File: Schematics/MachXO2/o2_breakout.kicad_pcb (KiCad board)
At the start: 2 copper layers, 95 x 72 mm, 94 parts, among them J1 Conn_02x20_Odd_Even, J2 Conn_02x20_Odd_Even, J3 USB_B_Micro, J4 DM3AT-SF-PEJM5, SW3 Reset, U1 LCMXO2-2000HC-4TG100C, U2 FT2232D, U3 TCM809, U4 93C56, U5 CY7C1010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

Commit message: Update Schematic
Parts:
- C6: moved to F.Cu
- U4: footprint Housings_SOIC:SO-8_5.3x6.2mm_Pitch1.27mm -> Housings_SOIC:SOIC-8_3.9x4.9mm_Pitch1.27mm
- U9: footprint Package_SO:SOIC-8_5.23x5.23mm_P1.27mm -> Housings_SOIC:SOIC-8_3.9x4.9mm_Pitch1.27mm
- moved R14 6.30 mm to (150.8, 103.9)
- moved C6 5.13 mm to (127.8, 71.1), turned to 180 degrees
- moved C16 3.36 mm to (191.2, 118.7), turned to 90 degrees
- moved R13 2.78 mm to (150.7, 94.1)
- moved U4 1.05 mm to (187.7, 114.8)
- moved C9 1.04 mm to (147.9, 95.1), turned to 90 degrees
- moved U9 0.93 mm to (151.9, 98.6)
- moved R16 0.52 mm to (181.3, 126.2)
- moved D2 0.52 mm to (179.7, 126.2)
- moved H5 0.17 mm to (146.0, 82.2)
- moved R8 0.09 mm to (147.2, 102.1), turned to 0 degrees
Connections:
- J1 pad 28: Net-(J1-Pad28) -> /GCLK1
- J1 pad 30: /GCLK1 -> GND
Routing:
- net Net-(R14-Pad2): track 8.01 -> 3.08 mm
- net +5V: track 93.4 -> 90.3 mm
- net Net-(R13-Pad2): track 4.34 -> 1.72 mm
- net /JTAG_TDI: track 86.5 -> 84.7 mm
- net /JTAG_TDO: track 88.4 -> 86.6 mm
- net /GCLK1: track 48.9 -> 47.8 mm
- net /JTAG_TCK: track 83.4 -> 82.4 mm
- net +3V3: track 473.3 -> 474.2 mm
- net /SPI_CS0: track 15.5 -> 16.3 mm
- net /SPI_MISO: track 113.1 -> 112.5 mm
- net GND: vias 206 -> 214
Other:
- board text added: "3V3"
- board text removed: "GND"

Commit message: Update PCB.
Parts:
- moved C16 0.28 mm to (191.2, 118.4)
- moved R14 0.27 mm to (150.8, 104.2)
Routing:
- net GND: vias 214 -> 215

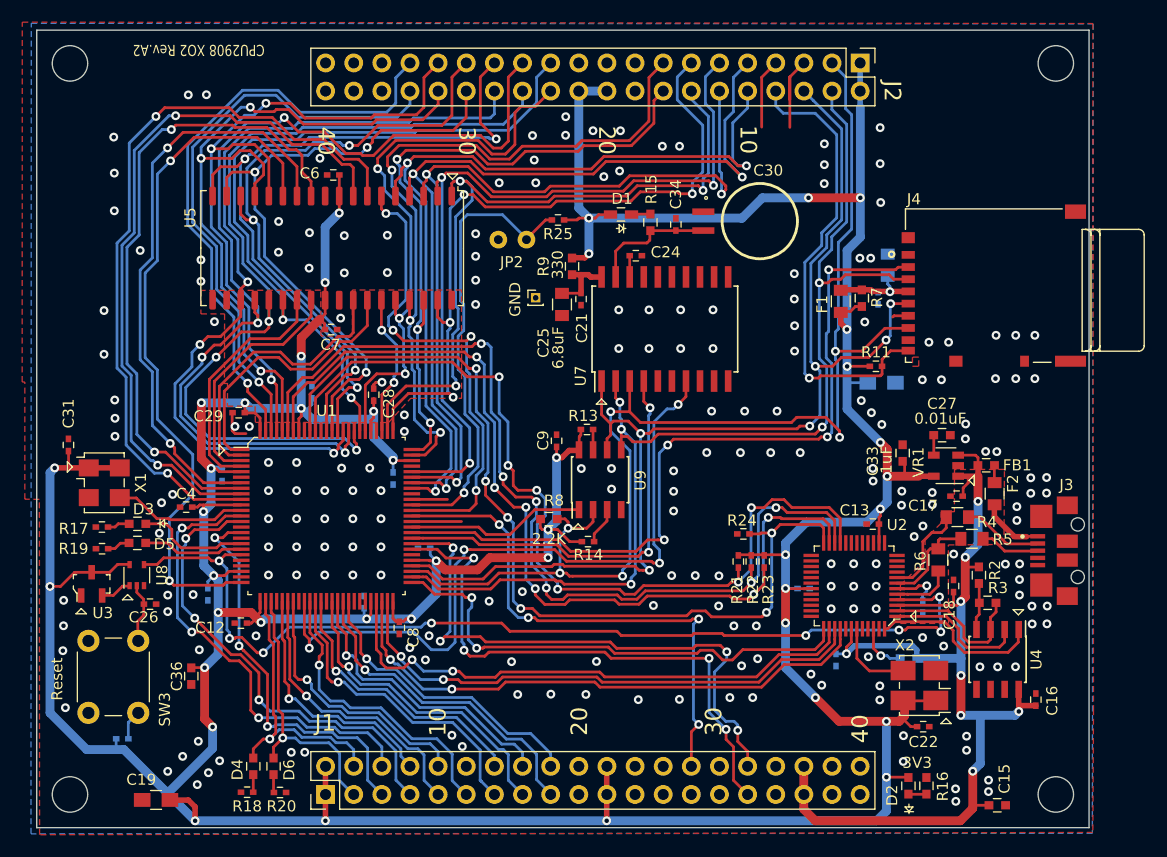
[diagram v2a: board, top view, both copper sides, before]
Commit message: Add schematic Rev C3.
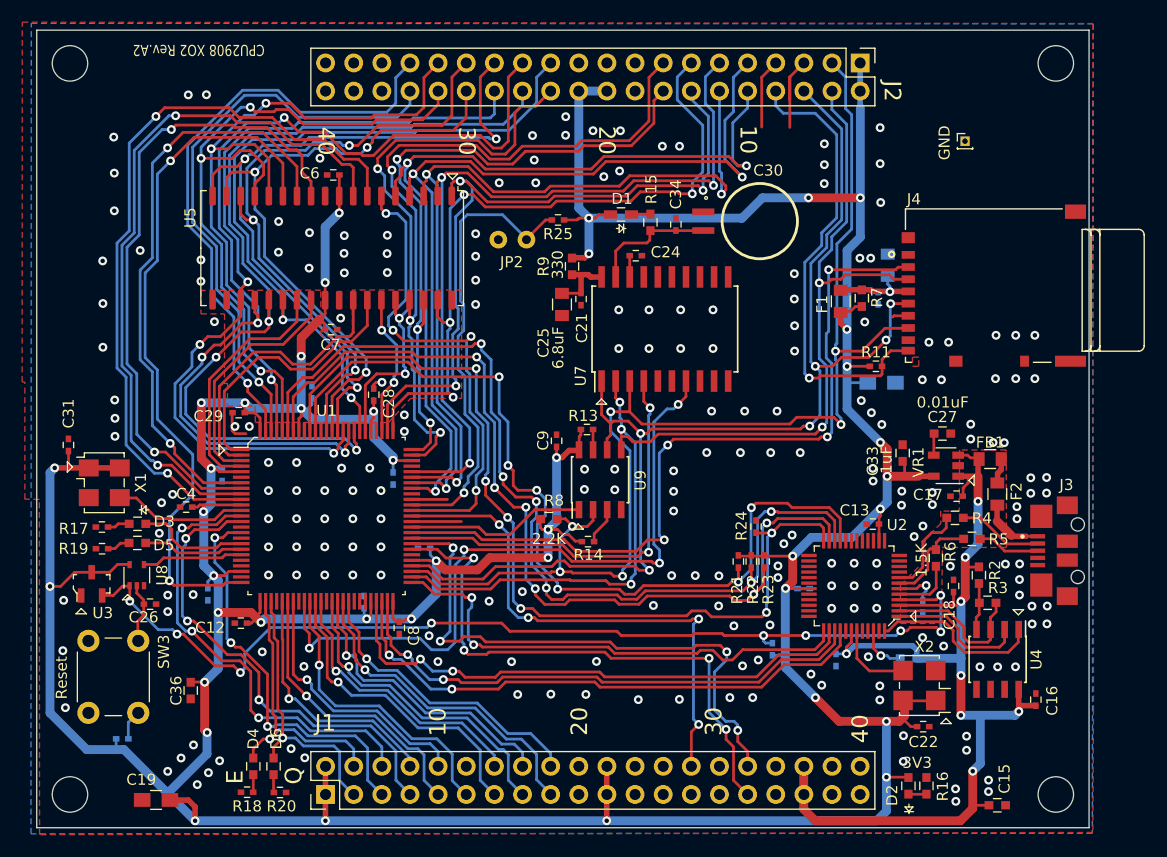
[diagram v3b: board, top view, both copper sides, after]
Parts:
- added R12: 10K, Capacitors_SMD:C_0402, B.Cu at (167.4, 113.9)
- FB1: footprint Capacitors_SMD:C_0603 -> Capacitors_SMD:C_0805
- R4, R5, R6: footprint Capacitors_SMD:C_0805 -> Capacitors_SMD:C_0603
- moved H5 41.3 mm to (184.8, 68.0)
- moved R24 1.31 mm to (165.9, 102.8), turned to 90 degrees
- moved C36 1.30 mm to (114.9, 117.6)
- moved FB1 0.66 mm to (187.1, 96.7)
- moved R6 0.28 mm to (182.2, 105.6)
- moved F2 0.24 mm to (187.7, 99.9)
- moved R4 0.23 mm to (183.9, 102.0)
- moved C27 0.15 mm to (182.8, 94.4)
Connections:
- U2 pad 4: /nReset -> /FT_Reset
- U3 pad 2: Net-(U3-Pad2) -> /FT_Reset
- U8 pad 1: Net-(U3-Pad2) -> /FT_Reset
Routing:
- net /FT_Reset: track 0.00 -> 92.4 mm, vias 0 -> 9
- net /nReset: track 90.9 -> 9.12 mm, vias 8 -> 0
- net Net-(U3-Pad2): track 2.72 -> 0.00 mm
- net /SPI_MISO: track 112.8 -> 111.2 mm
- net /RTC_CLK: track 64.5 -> 63.7 mm
- net /JTAG_TDO: track 86.3 -> 85.5 mm
- net /~CTS: track 50.2 -> 49.5 mm
- net /FT2232D/VBus: track 5.65 -> 4.95 mm
- net Net-(F2-Pad1): track 1.60 -> 2.20 mm
- net /S1: track 42.4 -> 42.9 mm
- net +3V3: track 474.3 -> 474.4 mm, vias 41 -> 40
- net GND: vias 215 -> 219
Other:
- board text added: "E"
- board text added: "Q"

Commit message: Update BreakOut Schematic.
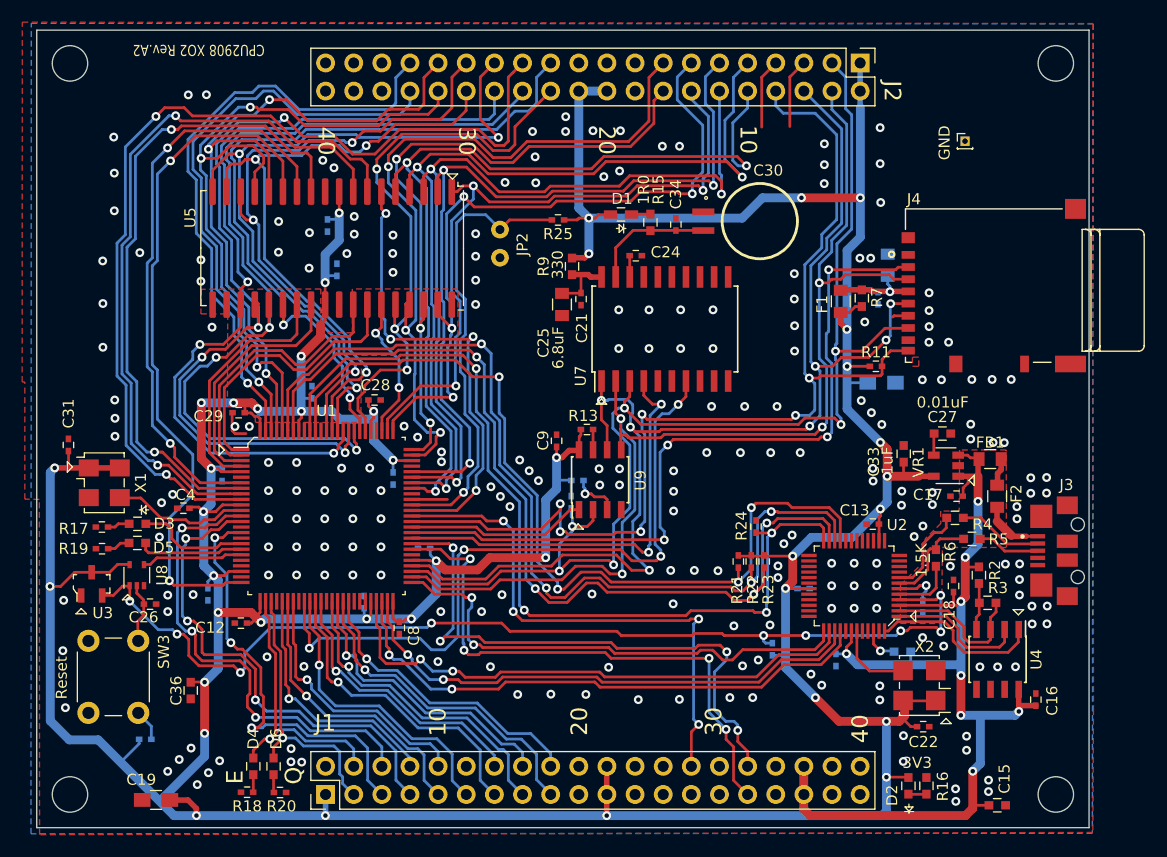
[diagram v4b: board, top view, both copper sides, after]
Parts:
- C6, C7, R14: moved to B.Cu
- R8: value 2.2K -> 10K; footprint Capacitors_SMD:C_0603 -> Capacitors_SMD:C_0402; moved to B.Cu
- moved R14 5.60 mm to (149.8, 98.7)
- moved C7 5.42 mm to (128.1, 79.6), turned to 90 degrees
- moved C6 4.60 mm to (127.2, 75.6), turned to 270 degrees
- moved JP2 2.56 mm to (142.8, 76.0), turned to 270 degrees
- moved R8 2.53 mm to (149.3, 100.6), turned to 270 degrees
- moved R10 2.07 mm to (110.8, 122.0)
- moved R1 0.82 mm to (179.1, 114.1)
- moved C28 0.49 mm to (131.5, 91.4), turned to 0 degrees
- moved C4 0.27 mm to (114.2, 101.2)
- moved F2 0.20 mm to (187.7, 100.1)
- moved C33 0.12 mm to (179.3, 96.2)
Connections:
- J1 pad 2: +3V3 -> GND
- J1 pad 20: Net-(J1-Pad20) -> GND
- U1 pad 62: Net-(U1-Pad62) -> /~SD_CD
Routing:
- net /~SD_CD: track 41.9 -> 96.7 mm, vias 1 -> 6
- net +3V3: track 474.4 -> 469.9 mm
- net Net-(U1-Pad62): track 4.49 -> 0.00 mm
- net /SPI_CLK: track 107.2 -> 111.6 mm, vias 6 -> 7
- net /A4: track 64.5 -> 61.9 mm
- net /A9: track 65.8 -> 68.1 mm
- net /~TSC: track 36.6 -> 38.8 mm
- net Net-(J2-Pad5): track 8.35 -> 6.27 mm
- net /A3: track 72.1 -> 73.9 mm
- net /A7: track 65.4 -> 67.1 mm
- net /nCS0: track 44.2 -> 42.6 mm
- net /A17: track 63.5 -> 65.1 mm
- net /A11: track 87.8 -> 89.4 mm
- net /S0: track 41.4 -> 42.9 mm
- net /A12: track 73.9 -> 75.4 mm
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
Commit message: Update Schematics
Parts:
- added C38: 0.1uF, Capacitors_SMD:C_0402, F.Cu at (104.3, 85.7)
- added D7: LED, Capacitors_SMD:C_0402, F.Cu at (167.9, 104.7)
- added D8: LED, Capacitors_SMD:C_0402, F.Cu at (169.0, 104.7)
- added R26: 10K, Capacitors_SMD:C_0402, B.Cu at (102.8, 95.4)
- added R27: 22K, Capacitors_SMD:C_0402, B.Cu at (167.8, 105.2)
- added R28: 22K, Capacitors_SMD:C_0402, B.Cu at (169.1, 105.2)
- added SW1: USER, Buttons_Switches_ThroughHole:SW_PUSH_6mm, F.Cu at (110.1, 75.9)
- moved R23 3.02 mm to (166.6, 109.0), turned to 180 degrees
- moved R21 2.33 mm to (166.6, 106.6), turned to 180 degrees
- moved R22 2.12 mm to (166.6, 107.8), turned to 180 degrees
- moved C7 1.87 mm to (128.2, 81.5), turned to 0 degrees
- moved JP2 1.28 mm to (144.1, 76.0)
- moved X1 1.14 mm to (107.4, 97.8)
- moved C13 1.12 mm to (177.6, 102.7), turned to 0 degrees
- moved C20 1.05 mm to (174.2, 115.0), turned to 180 degrees
- moved C12 0.99 mm to (118.5, 111.7)
- moved R24 0.89 mm to (166.2, 103.7), turned to 270 degrees
- moved R11 0.53 mm to (176.3, 88.2)
- moved C11 0.44 mm to (170.1, 108.8)
- moved C23 0.39 mm to (178.0, 78.9)
- moved C31 0.38 mm to (103.5, 95.4)
- moved R19 0.37 mm to (106.9, 105.2)
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- renumbered SW3 to SW2
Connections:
- net /UM1 renamed /IO9
- net /UM3 renamed /IO11
- net /nCS0 renamed /~CE
- net /nCS2 renamed /~CS2
- J1 pad 10: /UM2 -> /IO8
- J1 pad 12: GND -> /IO10
- J1 pad 13: /UM4 -> GND
- J1 pad 14: /UM5 -> GND
- J1 pad 15: /UM6 -> /IO13
- J1 pad 16: /UM7 -> /IO12
- J1 pad 17: /~nAltRD -> /IO15
- J1 pad 18: /~nAltWR -> /IO14
- J1 pad 19: GND -> /~nAltWR
- J1 pad 20: GND -> /~nAltRD
- J1 pad 8: /UM0 -> /~CS1
- J2 pad 10: /A0 -> /A2
- J2 pad 11: /A3 -> /A5
- J2 pad 12: /A2 -> /A4
- J2 pad 13: /A5 -> /A7
- J2 pad 14: /A4 -> /A6
- J2 pad 15: /A7 -> GND
- J2 pad 16: /A6 -> GND
- J2 pad 17: Net-(J2-Pad17) -> /A9
- J2 pad 18: Net-(J2-Pad18) -> /A8
- J2 pad 19: GND -> /A11
- J2 pad 20: +3V3 -> /A10
- J2 pad 21: GND -> /A13
- J2 pad 22: +3V3 -> /A12
- J2 pad 23: /A9 -> /A15
- J2 pad 24: /A8 -> /A14
- J2 pad 25: /A11 -> GND
- J2 pad 26: /A10 -> GND
- J2 pad 27: /A13 -> /A17
- J2 pad 28: /A12 -> /A16
- J2 pad 29: /A15 -> /A19
- J2 pad 30: /A14 -> /A18
- J2 pad 31: /A17 -> GND
- J2 pad 32: /A16 -> GND
- J2 pad 33: /A19 -> /IO1
- J2 pad 34: /A18 -> /IO0
- J2 pad 35: Net-(J2-Pad35) -> /IO3
- J2 pad 36: Net-(J2-Pad36) -> /IO2
- J2 pad 37: GND -> /IO5
- J2 pad 38: GND -> /IO4
- J2 pad 39: GND -> /IO7
- J2 pad 40: GND -> /IO6
- J2 pad 5: Net-(J2-Pad5) -> /~SD_CD
- J2 pad 7: Net-(J2-Pad7) -> /A1
- J2 pad 8: /~SD_CD -> /A0
- J2 pad 9: /A1 -> /A3
- R10 pad 2: Net-(C26-Pad1) -> Net-(R10-Pad2)
- SW2 pad 2: Net-(C26-Pad1) -> Net-(R10-Pad2)
- U1 pad 15: Net-(U1-Pad15) -> /USER
- U1 pad 29: Net-(U1-Pad29) -> /~CS1
- U1 pad 30: /UM0 -> /IO8
- U1 pad 32: /UM2 -> /IO10
- U1 pad 36: /UM4 -> /IO12
- U1 pad 37: /UM5 -> /IO13
- U1 pad 39: /UM6 -> /IO14
- U1 pad 40: /UM7 -> /IO15
- U2 pad 27: Net-(U2-Pad27) -> /FT2232D/~TxLED
- U2 pad 28: Net-(U2-Pad28) -> /FT2232D/~RxLED
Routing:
- net /IO4: track 22.5 -> 75.6 mm, vias 0 -> 1
- net /IO5: track 22.3 -> 74.7 mm, vias 0 -> 1
- net /IO7: track 25.8 -> 70.6 mm, vias 0 -> 2
- net /IO6: track 25.6 -> 69.6 mm, vias 0 -> 2
- net /IO1: track 64.6 -> 103.2 mm
- net /USER: track 0.00 -> 37.7 mm, vias 0 -> 2
- net /IO3: track 53.0 -> 90.4 mm, vias 2 -> 3
- net /IO2: track 59.3 -> 93.2 mm, vias 2 -> 3
- net /IO15: track 0.00 -> 33.5 mm, vias 0 -> 1
- net /IO13: track 0.00 -> 32.9 mm, vias 0 -> 1
- net /IO14: track 0.00 -> 30.3 mm, vias 0 -> 1
- net /IO12: track 0.00 -> 29.2 mm, vias 0 -> 1
- net /UM6: track 29.0 -> 0.00 mm, vias 1 -> 0
- net /UM4: track 28.4 -> 0.00 mm, vias 1 -> 0
- net /IO10: track 0.00 -> 27.4 mm, vias 0 -> 1
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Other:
- board text added: "Rx"
- board text added: "Tx"

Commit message: Update schematics
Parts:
- added R29: 10K, Capacitors_SMD:C_0402, B.Cu at (174.1, 94.7)
- C20: moved to F.Cu
- moved R12 62.7 mm to (104.9, 109.1), turned to 0 degrees
- moved C24 1.06 mm to (155.7, 77.5)
- moved C20 0.39 mm to (173.8, 115.0), turned to 270 degrees
- moved H6 0.10 mm to (194.9, 102.6)
- moved H7 0.10 mm to (194.9, 107.4)
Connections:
- net Net-(J4-Pad1) renamed /SDCARD/DAT2_NC
- net Net-(J4-Pad8) renamed /SDCARD/DAT1_NC
- J1 pad 23: Net-(J1-Pad23) -> GND
- J1 pad 24: Net-(J1-Pad24) -> GND
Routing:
- net /FT_Reset: track 92.8 -> 97.7 mm
- net /JTAG_TMS: track 81.7 -> 86.5 mm
- net +3V3: track 462.4 -> 465.6 mm
- net /JTAG_TCK: track 85.1 -> 87.7 mm
- net /JTAG_TDI: track 86.7 -> 88.9 mm
- net /JTAG_TDO: track 86.6 -> 88.7 mm
- net /SPI_CS1: track 69.6 -> 71.0 mm
- net Net-(C24-Pad1): track 1.90 -> 3.16 mm
- net +5V: track 90.8 -> 92.1 mm
- net /A10: track 91.1 -> 90.0 mm
- net /A1: track 77.7 -> 78.7 mm
- net /Boot: track 41.3 -> 42.2 mm
- net /SPI_MISO: track 109.3 -> 110.1 mm
- net /GCLK1: track 47.7 -> 48.5 mm
- net /A16: track 73.0 -> 72.2 mm
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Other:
- board text added: "AT"
- board text added: "Prototype area"
- board text added: "T"

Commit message: Clean up PCB.
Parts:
- removed C26: 0.1uF, Capacitors_SMD:C_0402
- added C39: 0.1uF, Capacitors_SMD:C_0402, F.Cu at (110.2, 122.6)
- added R30: 10K, Capacitors_SMD:C_0402, F.Cu at (147.7, 100.1)
- C19: moved to B.Cu
- C23: value 10uF -> 47uF
- JP2: footprint Wire_Connections_Bridges:WireConnection_0.80mmDrill -> Wire_Connections_Bridges:WireConnection_1.00mmDrill
- R7: value 1R0 -> 33; footprint Capacitors_SMD:C_0603 -> Capacitors_SMD:C_0805
- moved C19 6.65 mm to (118.4, 127.0), turned to 0 degrees
- moved C2 1.63 mm to (137.6, 104.7), turned to 90 degrees
- moved C15 0.63 mm to (187.7, 127.3)
- moved R7 0.51 mm to (176.0, 82.0)
- moved F1 0.50 mm to (173.8, 82.0)
- moved C36 0.19 mm to (114.7, 117.6)
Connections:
- J1 pad 33: Net-(J1-Pad33) -> +3V3
- J1 pad 34: Net-(J1-Pad34) -> +3V3
- J1 pad 37: GND -> Net-(J1-Pad37)
- J1 pad 38: GND -> Net-(J1-Pad38)
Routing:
- net +3V3: track 465.6 -> 469.8 mm
- net /SPI_CS0: track 16.3 -> 19.7 mm
- net Net-(C39-Pad1): track 2.88 -> 5.24 mm
- net /SPI_CS3: track 51.3 -> 49.5 mm
- net +5V: track 92.1 -> 90.4 mm
- net /A10: track 90.0 -> 91.3 mm
- net /A16: track 72.2 -> 73.0 mm
- net /A11: track 96.2 -> 96.9 mm
- net /SPI_CS1: track 71.0 -> 71.6 mm
- net /A9: track 76.6 -> 76.0 mm
- net /SDCARD/VddSD: track 8.96 -> 9.54 mm
- net /A13: track 72.9 -> 73.4 mm
- net GND: vias 209 -> 216

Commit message: V2
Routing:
- net /IO6: track 69.6 -> 69.0 mm
- net GND: vias 216 -> 227
